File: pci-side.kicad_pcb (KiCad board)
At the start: 2 copper layers, 170 x 48 mm, 16 parts, among them J1 PCIE-064-02-F-D-TH, P1 5622-4100-ML, U1 SFW30R-2STE1LF

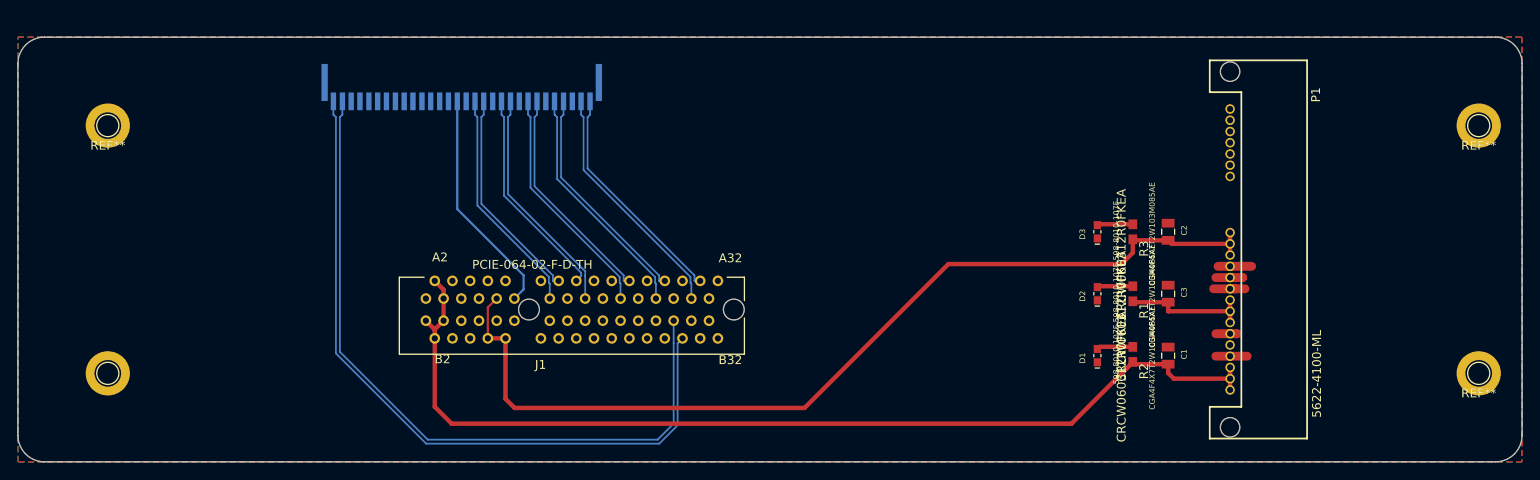
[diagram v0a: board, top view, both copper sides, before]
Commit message: better dPair routing, follow spec, move svg
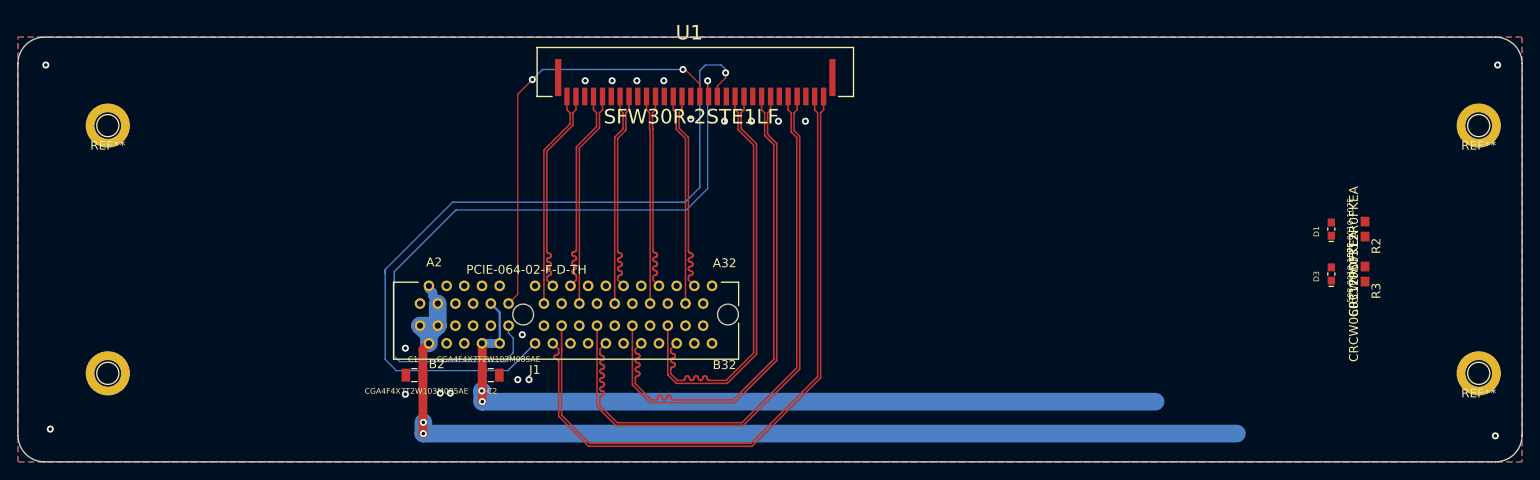
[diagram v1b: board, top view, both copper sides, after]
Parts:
- removed C3: CGA4F4X7T2W103M085AE, CGA4F4X7T2W103M085AE:CAPC2012X100N
- removed D2: 598-8010-107F, 598-8010-107F:LEDSC160X80X70L45N
- removed P1: 5622-4100-ML, 5622-4100-ML:3M_5622-4100-ML
- removed R1: CRCW060312R0FKEA, CRCW060312R0FKEA:0603
- U1: moved to F.Cu
- moved C1 85.2 mm to (114.8, 108.2), turned to 0 degrees
- moved C2 78.3 mm to (123.4, 108.2), turned to 180 degrees
- moved D1 30.1 mm to (218.4, 91.7)
- moved R2 29.8 mm to (222.2, 91.7)
- moved D3 26.9 mm to (218.4, 96.8)
- moved R3 26.7 mm to (222.2, 96.8)
- moved U1 26.4 mm to (146.6, 79.5), turned to 0 degrees
- moved J1 0.87 mm to (131.9, 101.3)
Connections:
- U1 pad 1: PET3- -> PET0+
- U1 pad 10: PET0- -> PET3+
- U1 pad 11: PET0+ -> PET3-
- U1 pad 12: Net-(U1-Pad12) -> GND
- U1 pad 13: WAKE# -> CLKREQ#
- U1 pad 14: CLKREQ# -> WAKE#
- U1 pad 17: REFCLK+ -> PER3-
- U1 pad 18: REFCLK- -> PER3+
- U1 pad 2: PET3+ -> PET0-
- U1 pad 20: PER0+ -> PER2-
- U1 pad 21: PER0- -> PER2+
- U1 pad 23: PER1+ -> PER1-
- U1 pad 24: PER1- -> PER1+
- U1 pad 26: PER2+ -> PER0-
- U1 pad 27: PER2- -> PER0+
- U1 pad 29: PER3+ -> REFCLK-
- U1 pad 3: Net-(U1-Pad3) -> GND
- U1 pad 30: PER3- -> REFCLK+
- U1 pad 4: PET2- -> PET1+
- U1 pad 5: PET2+ -> PET1-
- U1 pad 7: PET1- -> PET2+
- U1 pad 8: PET1+ -> PET2-
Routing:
- net CLKREQ#: track 0.00 -> 88.6 mm, vias 0 -> 1
- net WAKE#: track 0.00 -> 80.4 mm, vias 0 -> 1
- net PET0+: track 0.00 -> 76.2 mm
- net PET0-: track 0.00 -> 75.3 mm
- net PET1-: track 0.00 -> 66.8 mm
- net PET1+: track 0.00 -> 66.8 mm
- net PET2-: track 0.00 -> 56.2 mm
- net PET2+: track 0.00 -> 56.2 mm
- net PET3+: track 82.6 -> 47.3 mm
- net PET3-: track 82.4 -> 47.4 mm
- net PERST#: track 25.8 -> 47.9 mm, vias 0 -> 2
- net GND: track 16.9 -> 0.00 mm, vias 0 -> 20
- net +3V3: track 107.6 -> 90.9 mm, vias 0 -> 2
- net +5V: track 14.6 -> 0.00 mm
- net Net-(D1-PadA): track 4.10 -> 0.00 mm
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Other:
- net class Default: clearance 0.2 -> 0.254; trace_width 0.25 -> 0.1524
- net class dPair added: clearance 0.1524, trace_width 0.1524, via_dia 0.8, via_drill 0.4
- rule trace_clearance: 0.2 -> 0.254
- rule trace_min: 0.2 -> 0.12
